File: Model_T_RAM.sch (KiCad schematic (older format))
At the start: 3 parts, among them J1 KC-85_RAM, U1 6264, U2 74HC08

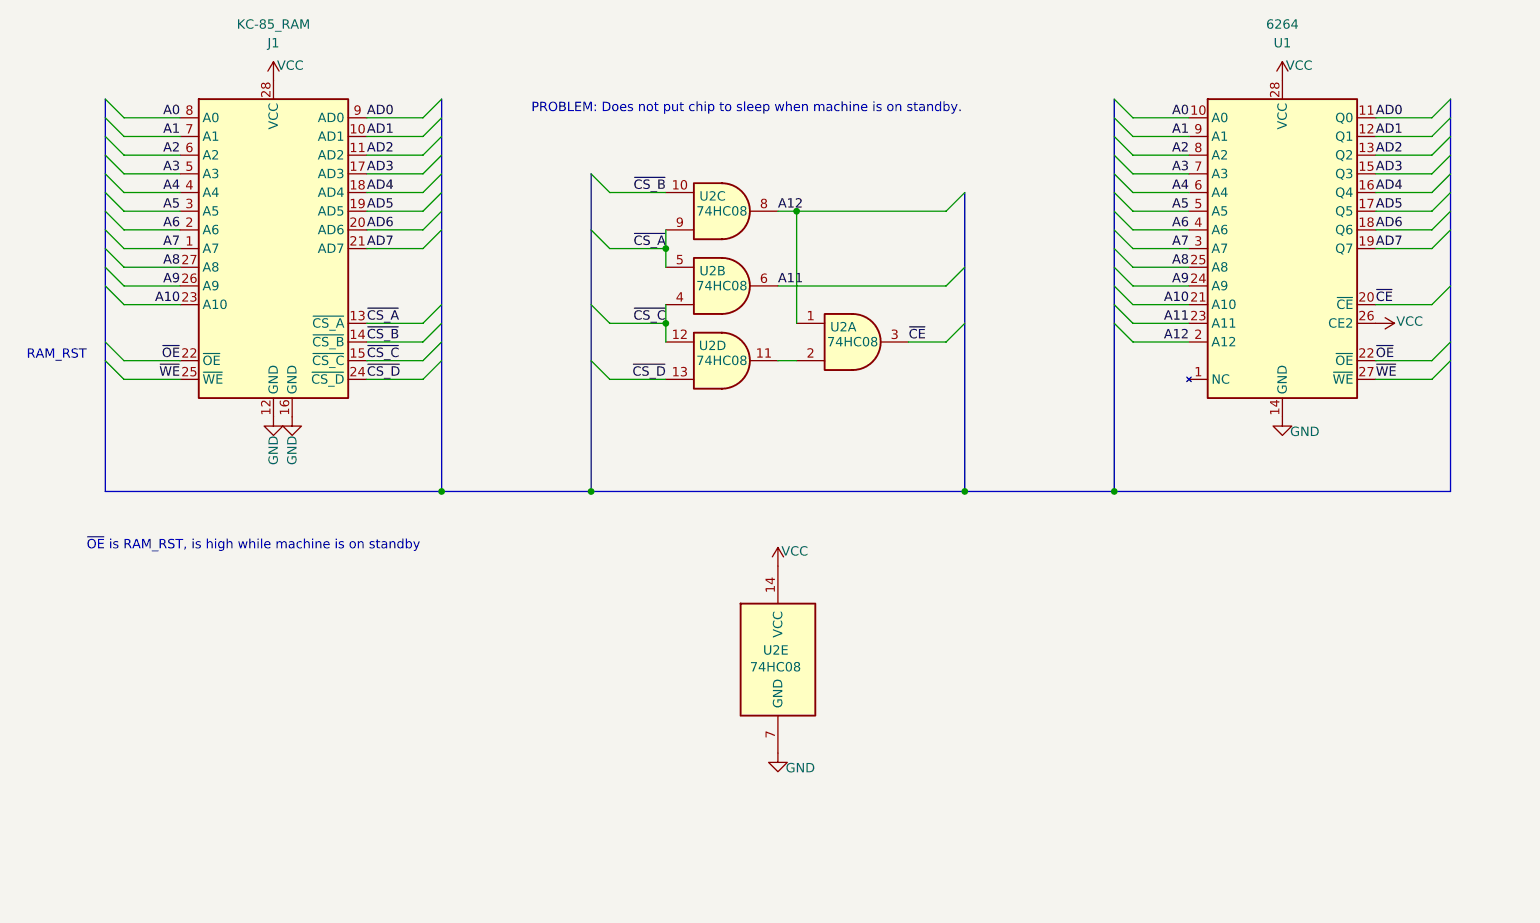
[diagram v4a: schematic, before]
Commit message: switch to 74HC86 to sleep on standby
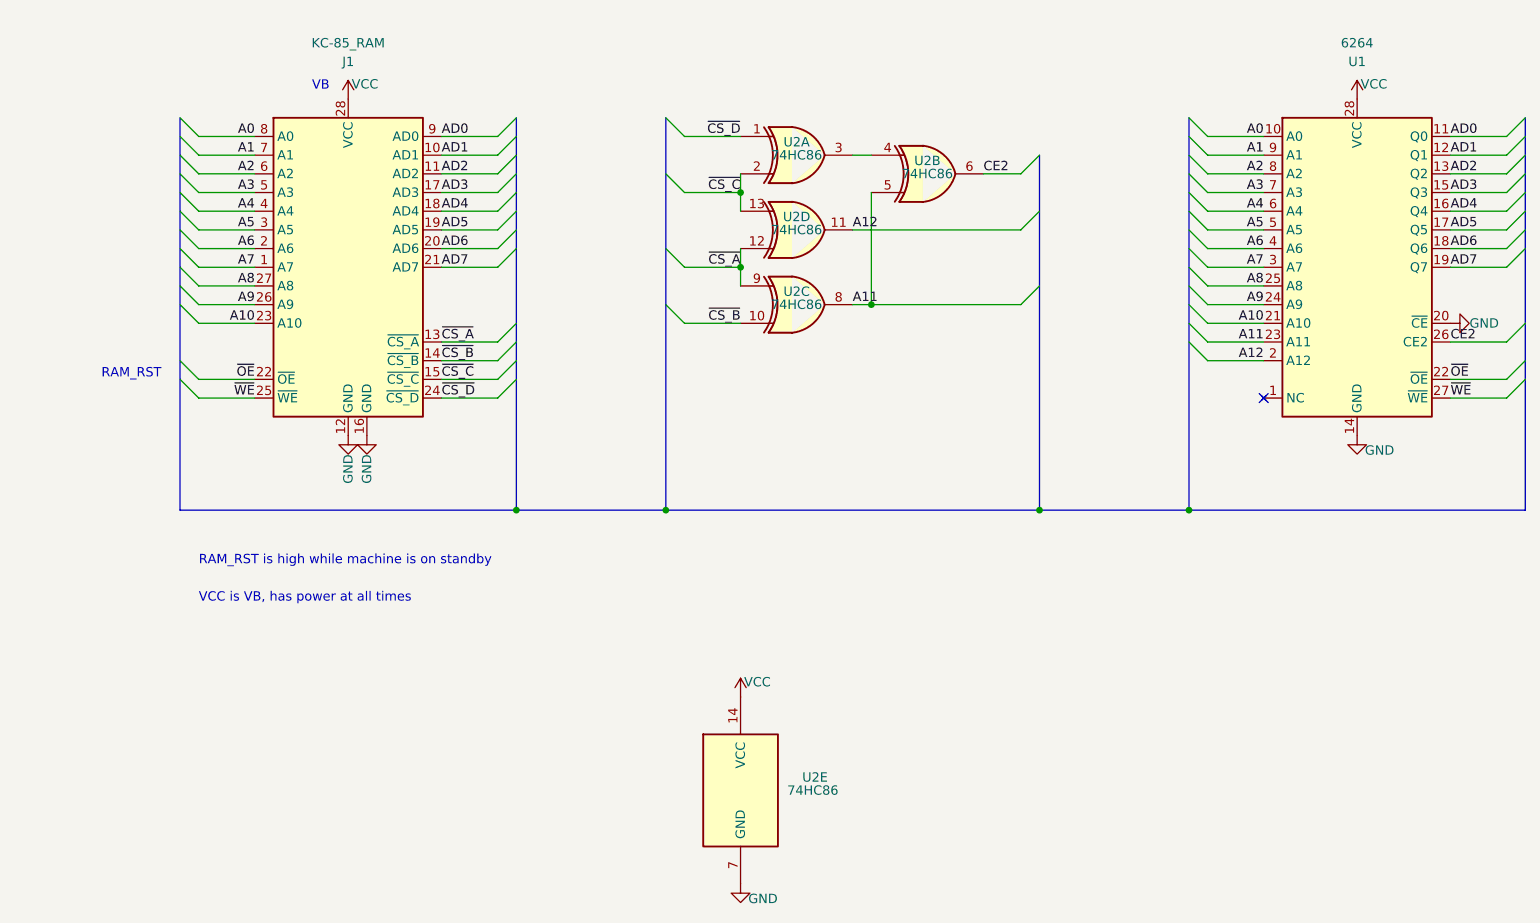
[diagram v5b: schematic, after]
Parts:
- removed U2: 74HC08, 000_LOCAL:SOIC-14_4x9, symbol 000_LOCAL:74HC08
- added U2: 74HC86, 000_LOCAL:SOIC-14_3.9x8.7mm_P1.27mm, symbol 000_LOCAL:74HC86
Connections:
- net ~CE is gone; now on net GND: U1.20 (~CE)
- net A11: now also U2.5, U2.8
- net A12: now also U2.11
- net GND: now also U2.7 (GND)
- net VCC: now also U2.14 (VCC); no longer U1.26 (CE2)
- net ~CS_A: now also U2.12, U2.9
- net ~CS_B: now also U2.10
- net ~CS_C: now also U2.13, U2.2
- net ~CS_D: now also U2.1
- new net: U2.3, U2.4
- new net CE2: U1.26 (CE2), U2.6
- no-connect marks 0 -> 1
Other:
- note added: "RAM_RST is high while machine is on standby"
- note added: "VB"
- note added: "VCC is VB, has power at all times"
- note removed: "PROBLEM: Does not put chip to sleep when machine is on standby."
- note removed: "~OE~ is RAM_RST, is high while machine is on standby"
- moved on the sheet: J1, U1

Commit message: rotate 7486
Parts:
- U2: footprint 000_LOCAL:SOIC-14_3.9x8.7mm_P1.27mm -> 000_LOCAL:SOIC-14_4x9
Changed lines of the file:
@@
 F 0 "U2" H 5300 3270 50  0000 C CNN
 F 1 "74HC86" H 5300 3200 50  0000 C CNN
-F 2 "000_LOCAL:SOIC-14_3.9x8.7mm_P1.27mm" H 5300 3200 50  0001 C CNN
+F 2 "000_LOCAL:SOIC-14_4x9" H 5300 3200 50  0001 C CNN
 F 3 "http://www.ti.com/lit/gpn/sn74HC86" H 5300 3200 50  0001 C CNN
 	1    5300 3200
@@
 F 0 "U2" H 5330 6670 50  0000 L CNN
 F 1 "74HC86" H 5250 6600 50  0000 L CNN
-F 2 "000_LOCAL:SOIC-14_3.9x8.7mm_P1.27mm" H 5000 6600 50  0001 C CNN
+F 2 "000_LOCAL:SOIC-14_4x9" H 5000 6600 50  0001 C CNN
 F 3 "http://www.ti.com/lit/gpn/sn74HC86" H 5000 6600 50  0001 C CNN
 	5    5000 6600
@@
 F 0 "U2" H 5300 4070 50  0000 C CNN
 F 1 "74HC86" H 5300 4000 50  0000 C CNN
-F 2 "000_LOCAL:SOIC-14_3.9x8.7mm_P1.27mm" H 5300 4000 50  0001 C CNN
+F 2 "000_LOCAL:SOIC-14_4x9" H 5300 4000 50  0001 C CNN
 F 3 "http://www.ti.com/lit/gpn/sn74HC86" H 5300 4000 50  0001 C CNN
 	3    5300 4000
@@
 F 0 "U2" H 5300 3530 50  0000 C CNN
 F 1 "74HC86" H 5300 3600 50  0000 C CNN
-F 2 "000_LOCAL:SOIC-14_3.9x8.7mm_P1.27mm" H 5300 3600 50  0001 C CNN
+F 2 "000_LOCAL:SOIC-14_4x9" H 5300 3600 50  0001 C CNN
 F 3 "http://www.ti.com/lit/gpn/sn74HC86" H 5300 3600 50  0001 C CNN
 	4    5300 3600
@@
 F 0 "U2" H 6000 3370 50  0000 C CNN
 F 1 "74HC86" H 6000 3300 50  0000 C CNN
-F 2 "000_LOCAL:SOIC-14_3.9x8.7mm_P1.27mm" H 6000 3300 50  0001 C CNN
+F 2 "000_LOCAL:SOIC-14_4x9" H 6000 3300 50  0001 C CNN
 F 3 "http://www.ti.com/lit/gpn/sn74HC86" H 6000 3300 50  0001 C CNN
 	2    6000 3300

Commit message: RAM_RST on /CE instead of /OE
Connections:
- net GND: now also U1.22 (~OE); no longer U1.20 (~CE)
- net ~OE renamed RAM_RST
- net RAM_RST: now also U1.20 (~CE); no longer U1.22 (~OE)
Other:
- note added: "/OE"
- note removed: "RAM_RST"
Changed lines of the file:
@@
 Title "Model T RAM Module"
 Date "2021-08-05"
-Rev "004"
+Rev "005"
 Comp "b.kenyon.w@gmail.com"
 Comment1 ""
@@
 Entry Wire Line
 	9100 4200 9200 4100
-Wire Wire Line
-	8800 4400 9100 4400
-Entry Wire Line
-	9100 4400 9200 4300
 Wire Wire Line
 	8800 4500 9100 4500
@@
 Text Label 5600 3600 0    50   ~ 0
 A12
-Text Label 8800 4200 0    50   ~ 0
-CE2
-$Comp
-L power:GND #PWR0107
-U 1 1 609A2377
-P 8800 4100
-F 0 "#PWR0107" H 8800 3850 50  0001 C CNN
-F 1 "GND" V 8800 3920 50  0000 C CNN
-F 2 "" H 8800 4100 50  0001 C CNN
-F 3 "" H 8800 4100 50  0001 C CNN
-	1    8800 4100
-	0    -1   -1   0
-$EndComp
 $Comp
 L 000_LOCAL:74HC86 U2
@@
 Text Label 2400 4100 2    50   ~ 0
 A10
-Text Label 2400 4400 2    50   ~ 0
-~OE
 Text Label 2400 4500 2    50   ~ 0
 ~WE
@@
 Text Label 8800 3800 0    50   ~ 0
 AD7
-Text Label 8800 4400 0    50   ~ 0
-~OE
 Text Label 8800 4500 0    50   ~ 0
 ~WE
@@
 Connection ~ 4600 5100
 Text Notes 1900 4400 2    50   ~ 0
-RAM_RST
+/OE
 Text Notes 2100 5400 0    50   ~ 0
 RAM_RST is high while machine is on standby
@@
 Wire Bus Line
 	6600 5100 7400 5100
+Wire Wire Line
+	8800 4100 9100 4100
+Entry Wire Line
+	9100 4100 9200 4000
+Text Label 8800 4200 0    50   ~ 0
+CE2
+Text Label 8800 4100 0    50   ~ 0
+RAM_RST
+$Comp
+L power:GND #PWR0107
+U 1 1 609A2377
+P 8800 4400
+F 0 "#PWR0107" H 8800 4150 50  0001 C CNN
+F 1 "GND" V 8800 4220 50  0000 C CNN
+F 2 "" H 8800 4400 50  0001 C CNN
+F 3 "" H 8800 4400 50  0001 C CNN
+	1    8800 4400
+	0    -1   -1   0
+$EndComp
+Text Label 2400 4400 2    50   ~ 0
+RAM_RST
 Wire Bus Line
 	6600 3200 6600 5100

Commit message: decoupling and ground pour
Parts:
- added C1, C2: 0.1u, 000_LOCAL:C_0805, symbol 000_LOCAL:C
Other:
- note added: "Optional decoupling"
- note added: "VCC is "VB", and has power at all times.\n\nRAM_RST is high while machine is on standby."
- note removed: "/OE"
- note removed: "RAM_RST is high while machine is on standby"
- note removed: "VCC is VB, has power at all times"
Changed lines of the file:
@@
 Sheet 1 1
 Title "Model T RAM Module"
-Date "2021-08-05"
-Rev "005"
+Date "2021-08-19"
+Rev "006"
 Comp "b.kenyon.w@gmail.com"
 Comment1 ""
@@
 	4600 4000 4700 4100
 Connection ~ 4600 5100
-Text Notes 1900 4400 2    50   ~ 0
-/OE
-Text Notes 2100 5400 0    50   ~ 0
-RAM_RST is high while machine is on standby
-Text Notes 2100 5600 0    50   ~ 0
-VCC is VB, has power at all times
+Text Notes 2100 5500 0    50   ~ 0
+VCC is "VB", and has power at all times.\n\nRAM_RST is high while machine is on standby.
 Text Notes 2800 2860 2    50   ~ 0
 VB
@@
 Text Label 2400 4400 2    50   ~ 0
 RAM_RST
+$Comp
+L 000_LOCAL:C C2
+U 1 1 611FFB62
+P 3960 6550
+F 0 "C2" H 4050 6590 50  0000 L CNN
+F 1 "0.1u" H 4050 6500 50  0000 L CNN
+F 2 "000_LOCAL:C_0805" H 3960 6550 50  0001 C CNN
+F 3 "~" H 3960 6550 50  0001 C CNN
+	1    3960 6550
+	1    0    0    -1
+$EndComp
+$Comp
+L power:VCC #PWR0109
+U 1 1 6120042F
+P 3960 6450
+F 0 "#PWR0109" H 3960 6300 50  0001 C CNN
+F 1 "VCC" H 4050 6530 50  0000 C CNN
+F 2 "" H 3960 6450 50  0001 C CNN
+F 3 "" H 3960 6450 50  0001 C CNN
+	1    3960 6450
+	1    0    0    -1
+$EndComp
+$Comp
+L power:GND #PWR0110
+U 1 1 6120103B
+P 3960 6650
+F 0 "#PWR0110" H 3960 6400 50  0001 C CNN
+F 1 "GND" H 4080 6570 50  0000 C CNN
+F 2 "" H 3960 6650 50  0001 C CNN
+F 3 "" H 3960 6650 50  0001 C CNN
+	1    3960 6650
+	1    0    0    -1
+$EndComp
+Text Notes 3430 6910 0    50   ~ 0
+Optional decoupling
+$Comp
+L 000_LOCAL:C C1
+U 1 1 6120A490
+P 3560 6550
+F 0 "C1" H 3650 6590 50  0000 L CNN
+F 1 "0.1u" H 3650 6500 50  0000 L CNN
+F 2 "000_LOCAL:C_0805" H 3560 6550 50  0001 C CNN
+F 3 "~" H 3560 6550 50  0001 C CNN
+	1    3560 6550
+	1    0    0    -1
+$EndComp
+$Comp
+L power:VCC #PWR0111
+U 1 1 6120A62C
+P 3560 6450
+F 0 "#PWR0111" H 3560 6300 50  0001 C CNN
+F 1 "VCC" H 3650 6530 50  0000 C CNN
+F 2 "" H 3560 6450 50  0001 C CNN
+F 3 "" H 3560 6450 50  0001 C CNN
+	1    3560 6450
+	1    0    0    -1
+$EndComp
+$Comp
+L power:GND #PWR0112
+U 1 1 6120A636
+P 3560 6650
+F 0 "#PWR0112" H 3560 6400 50  0001 C CNN
+F 1 "GND" H 3680 6570 50  0000 C CNN
+F 2 "" H 3560 6650 50  0001 C CNN
+F 3 "" H 3560 6650 50  0001 C CNN
+	1    3560 6650
+	1    0    0    -1
+$EndComp
 Wire Bus Line
 	6600 3200 6600 5100
